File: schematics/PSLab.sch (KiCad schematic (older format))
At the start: 101 parts, among them J1 DoublePins, J11 Li-Ion Battery, J3 Bluetooth, J4 I2C, J5 I2C, J6 ESP01, J7 UART/ESP, J9 SPI, P1 SDCard, Q2 MMBT3904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

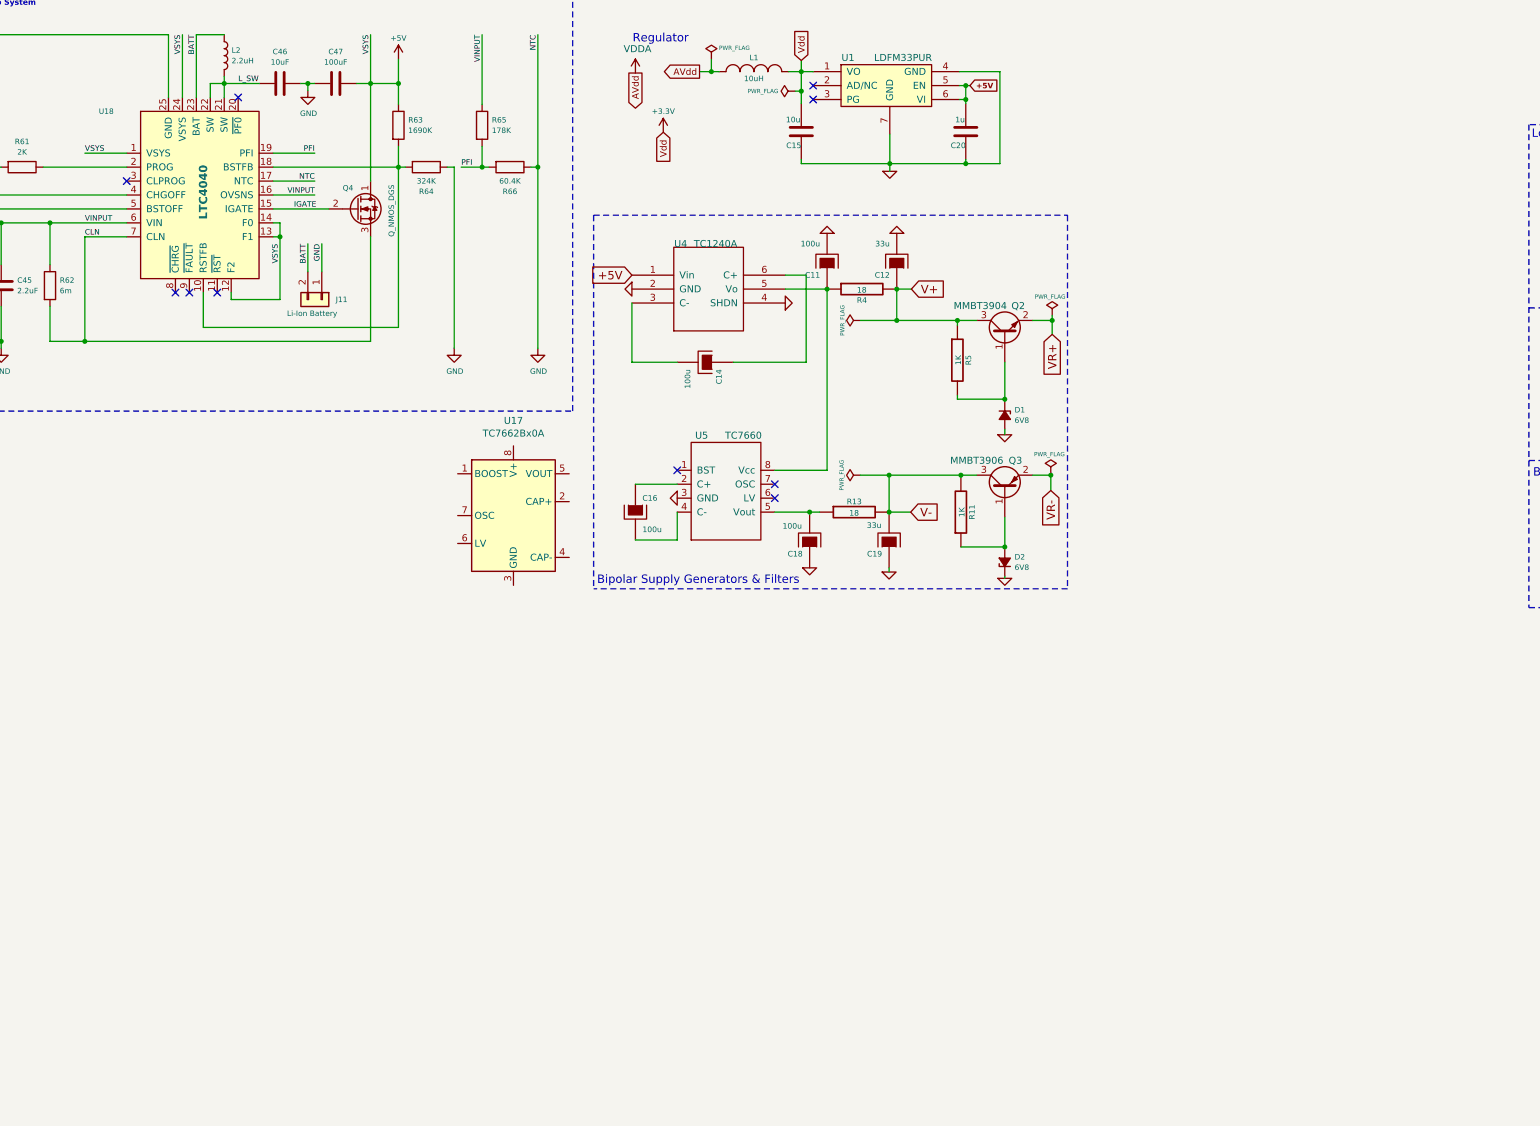
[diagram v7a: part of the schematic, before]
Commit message: refactor: redraw TC1280
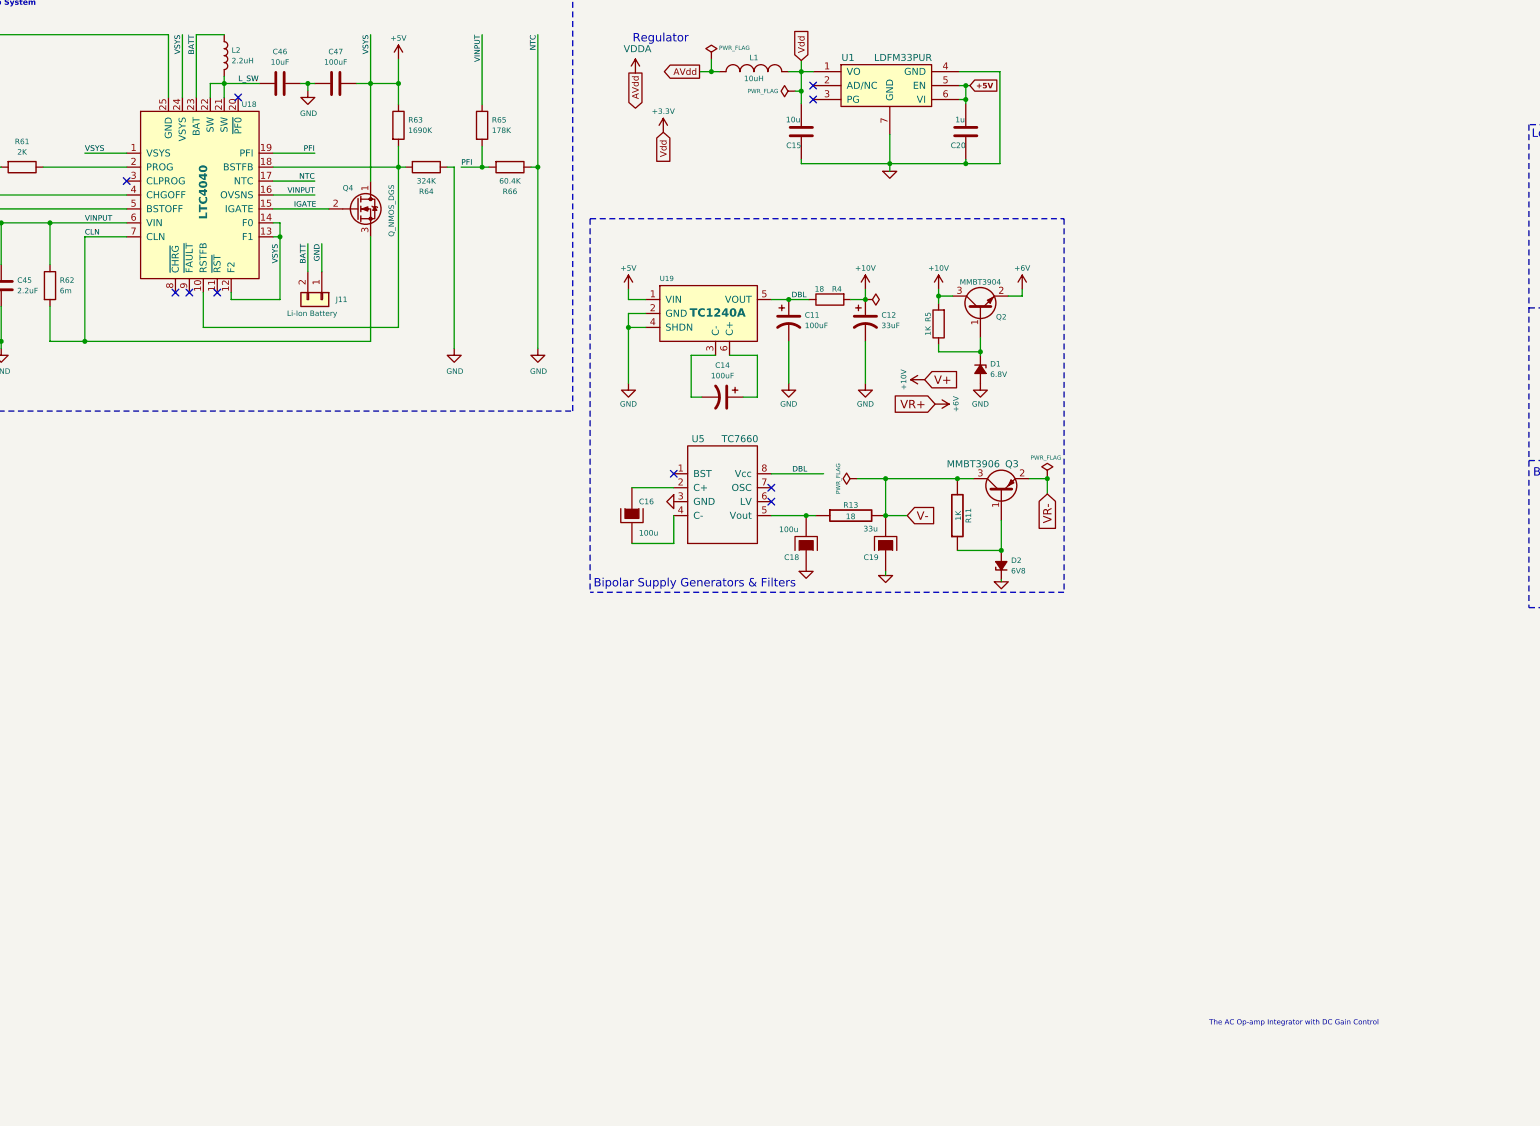
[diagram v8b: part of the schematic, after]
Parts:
- removed C11, C14: 100u, Capacitors_Tantalum_SMD:CP_Tantalum_Case-C_EIA-6032-28_Reflow, symbol PSLab-rescue:CAPAPOL
- removed C12: 33u, Capacitors_Tantalum_SMD:CP_Tantalum_Case-B_EIA-3528-21_Reflow, symbol PSLab-rescue:CAPAPOL
- removed Q2: MMBT3904, TO_SOT_Packages_SMD:SOT-23, symbol Transistor_BJT:MMBT3904
- removed R4: 18, Resistor_SMD:R_0603_1608Metric, symbol PSLab-rescue:R-RESCUE-proto1
- removed R5: 1K, Resistor_SMD:R_0603_1608Metric, symbol PSLab-rescue:R-RESCUE-proto1
- removed U17: TC7662Bx0A, Package_SO:SOIC-8_3.9x4.9mm_P1.27mm, symbol Converter_DCDC:TC7662Bx0A
- removed U4: TC1240A, Package_TO_SOT_SMD:SOT-23-6, symbol PSLab-rescue:TC1240A
- added C11, C14: 100uF, Capacitor_Tantalum_SMD:CP_EIA-6032-28_Kemet-C, symbol Device:CP1
- added C12: 33uF, Capacitor_Tantalum_SMD:CP_EIA-3528-21_Kemet-B, symbol Device:CP1
- added Q2: MMBT3904, TO_SOT_Packages_SMD:SOT-23, symbol Device:Q_NPN_BEC
- added R4: 18, Resistor_SMD:R_0603_1608Metric, symbol Device:R
- added R5: 1K, Resistor_SMD:R_0603_1608Metric, symbol PSLab-rescue:R
- added U19: TC1240A, Package_TO_SOT_SMD:SOT-23-6, symbol PSLab:TC1240A
- C16, C18: footprint Capacitors_Tantalum_SMD:CP_Tantalum_Case-C_EIA-6032-28_Reflow -> Capacitor_Tantalum_SMD:CP_EIA-6032-28_Kemet-C
- C47: Description (none) -> Tantalum 16V 6032-28; Mfr No. (none) -> F931C107KCC; PartNumber (none) -> F931C107KCC; Price (none) -> 1.29
- D1: value 6V8 -> 6.8V
- MH2, MH3, MH4: footprint Mounting_Holes:MountingHole_3.2mm_M3_DIN965_Pad -> MountingHole:MountingHole_3.2mm_M3_DIN965_Pad
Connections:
- net +5V: now also U19.1 (VIN)
- net GND: now also C11.2, C12.2, U19.2 (GND), U19.4 (SHDN)
- net DBL: now reaches U5.8 (Vcc)
- net DBL: now also C11.1, R4.1, U19.5 (VOUT)
- net at D1.1 (K): now also Q2.1 (B), R5.1
- new net: C14.2, U19.3 (C-)
- new net: C14.1, U19.6 (C+)
- new net +10V: C12.1, Q2.3 (C), R4.2, R5.2
- new net +6V: Q2.2 (E)
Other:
- note added: "The AC Op-amp Integrator with DC Gain Control\n\n"
- moved on the sheet: C16, C18, C19, D2, Q3, R11, R13, U5
